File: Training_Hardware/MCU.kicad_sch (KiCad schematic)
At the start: 3 parts, among them J1 RJ45_LED_Shielded, U1 Teensy4.1_DEV-16771

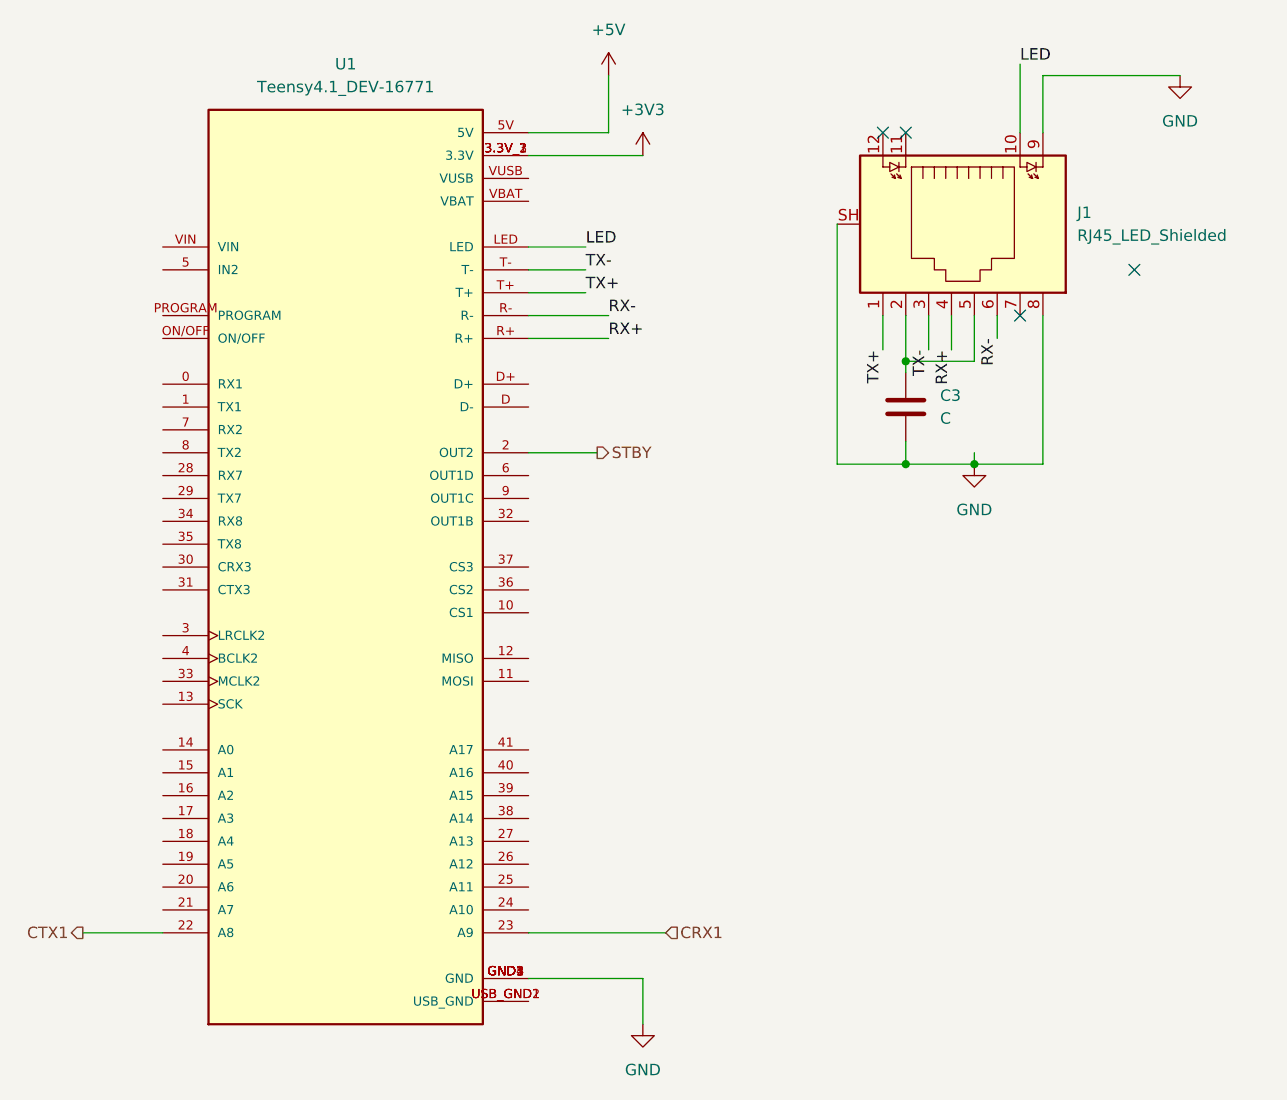
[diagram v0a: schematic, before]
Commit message: added Footprints
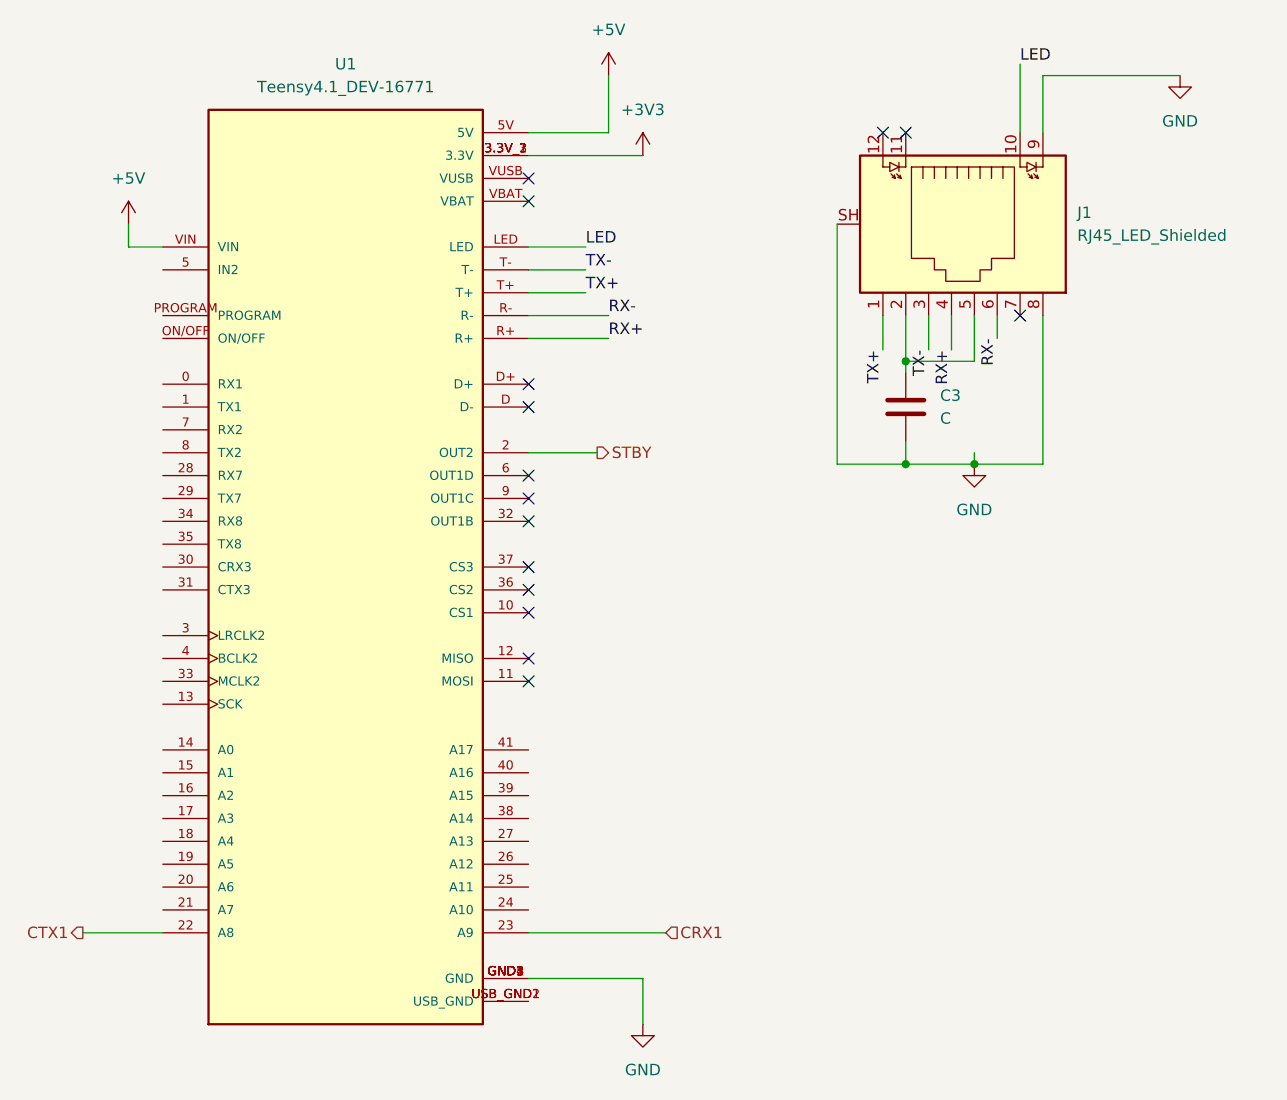
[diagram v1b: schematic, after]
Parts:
- C3: footprint (none) -> Capacitor_SMD:C_0603_1608Metric_Pad1.08x0.95mm_HandSolder
- J1: footprint (none) -> MRDT_Connectors:RJ45_Teensy
- U1: footprint MODULE_DEV-16771 -> MRDT_Shields:Teensy_4_1_Ethernet
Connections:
- net +5V: now also U1.VIN
- no-connect marks 4 -> 15
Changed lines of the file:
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@@
 	)
 	(no_connect
-		(at 156.21 58.42)
+		(at 88.9 86.36)
 	)
 	(no_connect
@@
 		(at 128.27 43.18)
 	)
+	(no_connect
+		(at 88.9 48.26)
+	)
+	(no_connect
+		(at 88.9 71.12)
+	)
+	(no_connect
+		(at 88.9 91.44)
+	)
+	(no_connect
+		(at 88.9 93.98)
+	)
+	(no_connect
+		(at 88.9 73.66)
+	)
+	(no_connect
+		(at 88.9 101.6)
+	)
+	(no_connect
+		(at 88.9 104.14)
+	)
+	(no_connect
+		(at 88.9 96.52)
+	)
+	(no_connect
+		(at 88.9 83.82)
+	)
+	(no_connect
+		(at 88.9 81.28)
+	)
+	(no_connect
+		(at 88.9 50.8)
+	)
 	(wire
 		(pts
@@
 		(pts
 			(xy 123.19 53.34) (xy 123.19 80.01)
+		)
+		(stroke
+			(width 0)
+			(type default)
+		)
+	)
+	(wire
+		(pts
+			(xy 44.45 53.34) (xy 44.45 55.88)
+		)
+		(stroke
+			(width 0)
+			(type default)
+		)
+	)
+	(wire
+		(pts
+			(xy 44.45 55.88) (xy 48.26 55.88)
 		)
 		(stroke
@@
 			)
 		)
-		(property "Footprint" "MODULE_DEV-16771"
+		(property "Footprint" "MRDT_Shields:Teensy_4_1_Ethernet"
 			(at 121.92 99.06 0)
 			(effects
@@
 	)
 	(symbol
+		(lib_id "power:+5V")
+		(at 44.45 53.34 0)
+		(unit 1)
+		(exclude_from_sim no)
+		(in_bom yes)
+		(on_board yes)
+		(dnp no)
+		(fields_autoplaced yes)
+		(property "Reference" "#PWR017"
+			(at 44.45 57.15 0)
+			(effects
+				(font
+					(size 1.27 1.27)
+				)
+				(hide yes)
+			)
+		)
+		(property "Value" "+5V"
+			(at 44.45 48.26 0)
+			(effects
+				(font
+					(size 1.27 1.27)
+				)
+			)
+		)
+		(property "Footprint" ""
+			(at 44.45 53.34 0)
+			(effects
+				(font
+					(size 1.27 1.27)
+				)
+				(hide yes)
+			)
+		)
+		(property "Datasheet" ""
+			(at 44.45 53.34 0)
+			(effects
+				(font
+					(size 1.27 1.27)
+				)
+				(hide yes)
+			)
+		)
+		(property "Description" "Power symbol creates a global label with name \"+5V\""
+			(at 44.45 53.34 0)
+			(effects
+				(font
+					(size 1.27 1.27)
+				)
+				(hide yes)
+			)
+		)
+		(pin "1"
+		)
+		(instances
+			(project "Training_Hardware"
+				(path "/11bb8091-1487-4100-afd2-5aa288c40d4f/bab747f3-bfff-4257-8440-bff62be5f0b7"
+					(reference "#PWR017")
+					(unit 1)
+				)
+			)
+		)
+	)
+	(symbol
 		(lib_id "power:GND")
 		(at 161.29 36.83 0)
@@
 			)
 		)
-		(property "Footprint" ""
+		(property "Footprint" "MRDT_Connectors:RJ45_Teensy"
 			(at 136.525 53.34 90)
 			(effects
@@
 			)
 		)
-		(property "Footprint" ""
+		(property "Footprint" "Capacitor_SMD:C_0603_1608Metric_Pad1.08x0.95mm_HandSolder"
 			(at 131.7752 77.47 0)
 			(effects
